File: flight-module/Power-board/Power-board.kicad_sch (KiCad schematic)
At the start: 26 parts, among them J5 POWER, J8 XT60-M, U1 AZ1117IH-3.3TRG1, U3 TPS4H160BQPWPRQ1, U4 AZ1117IH-5TRG1

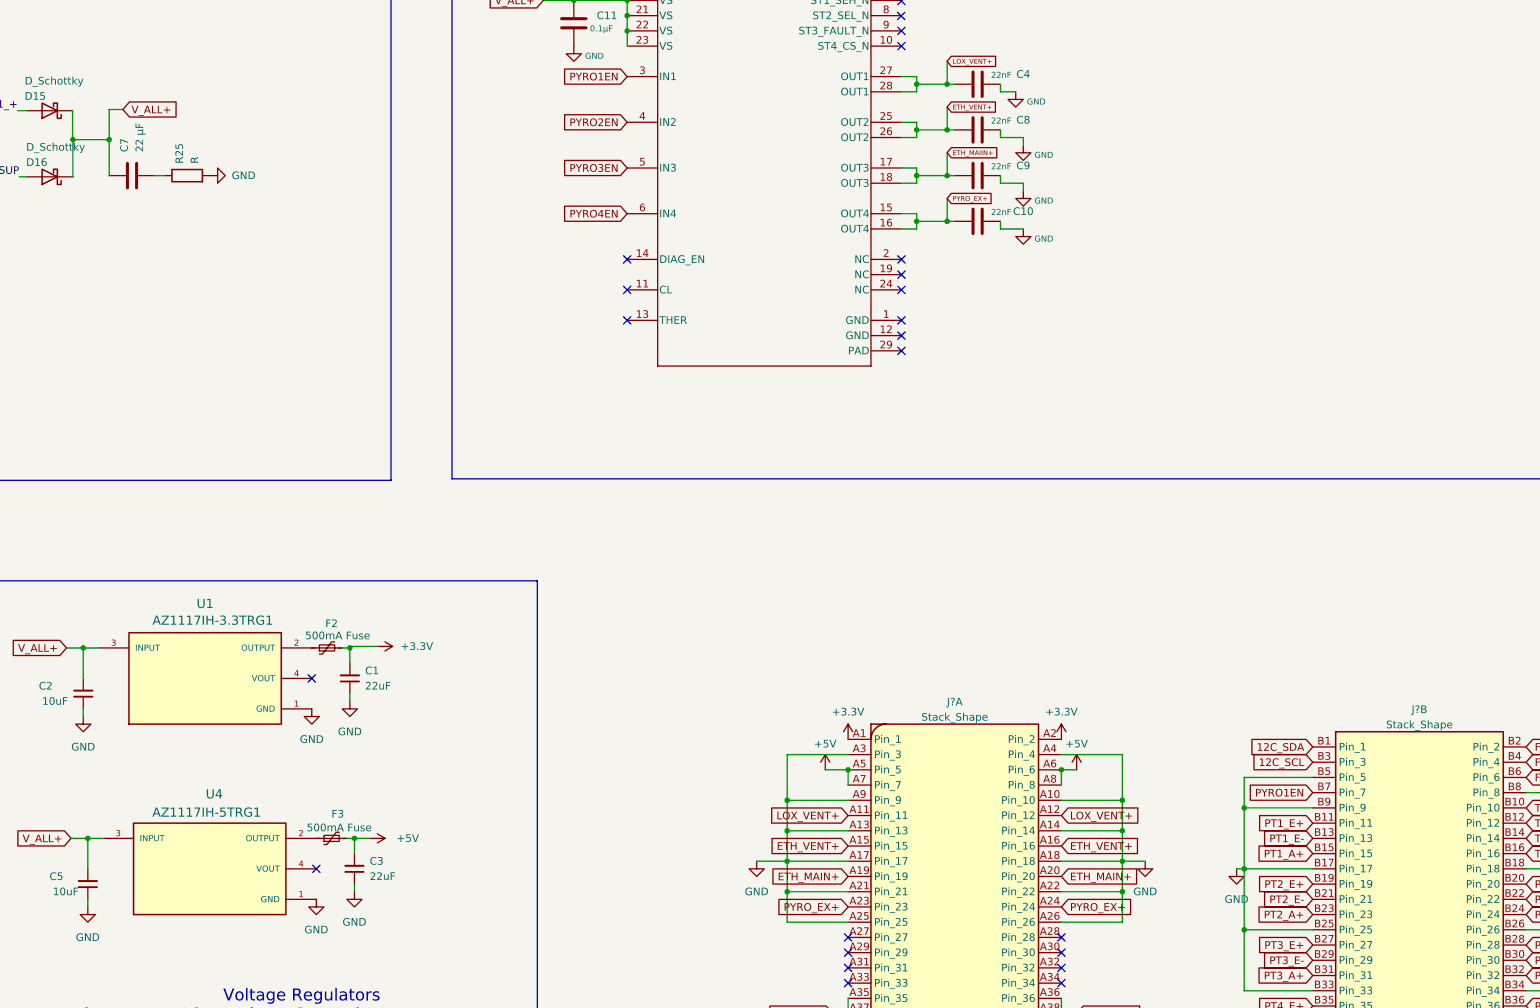
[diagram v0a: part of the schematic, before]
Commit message: added gnd to new ic on power board
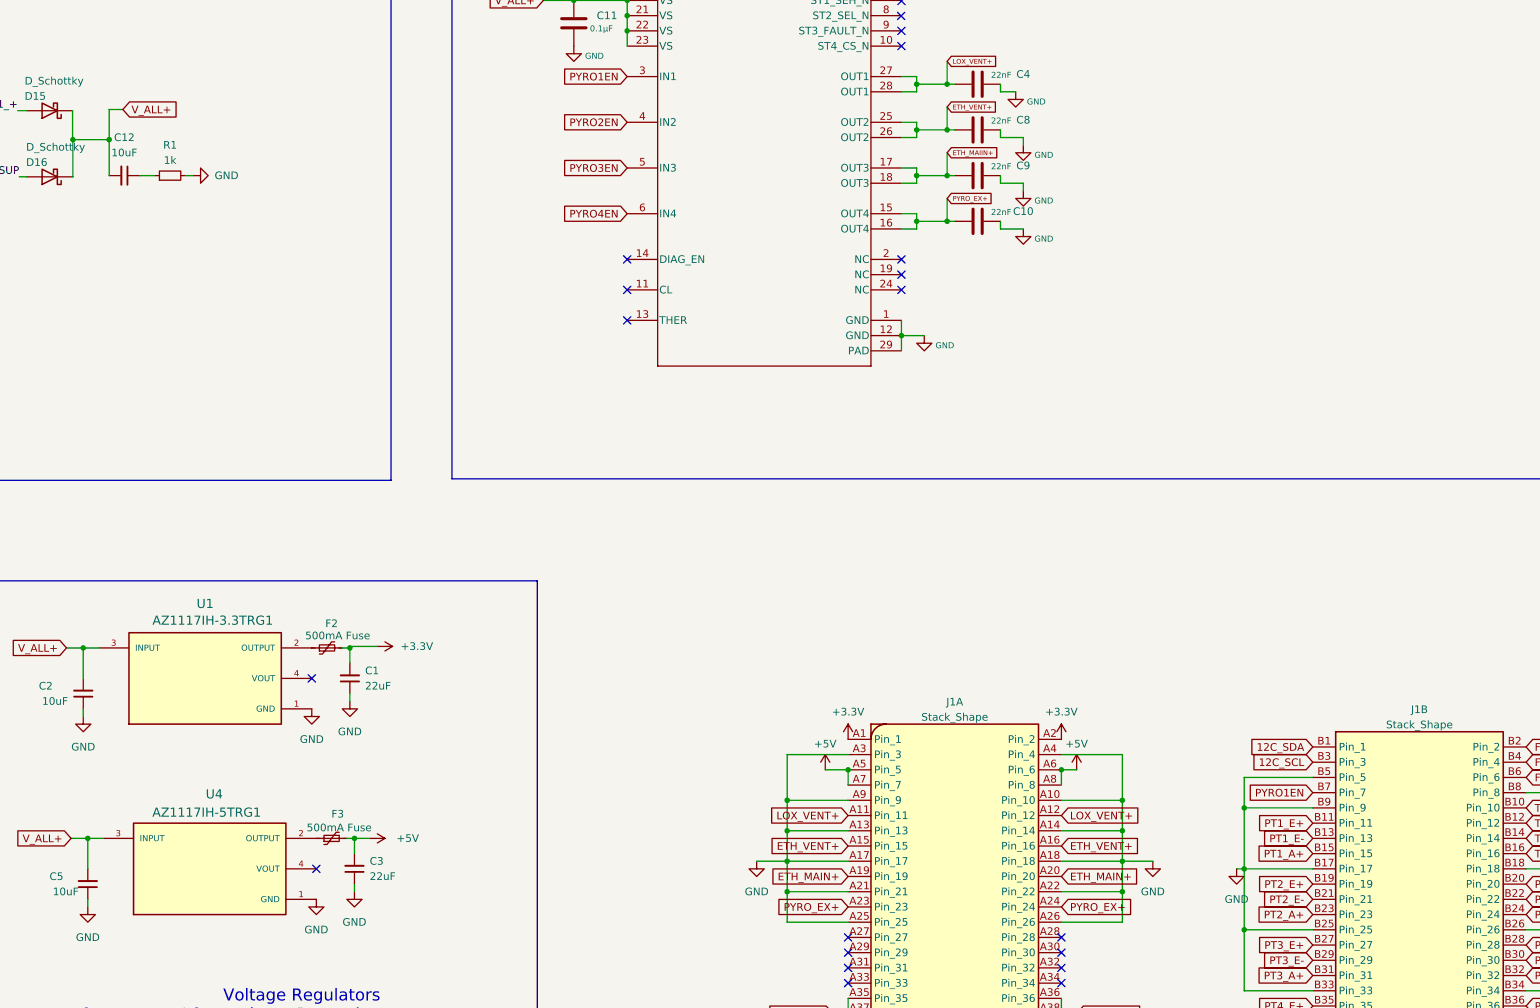
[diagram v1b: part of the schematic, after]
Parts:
- removed C7: 22 µF, symbol Device:C
- removed R25: R, symbol Device:R
- added C12: 10uF, Capacitor_SMD:C_0603_1608Metric, symbol Device:C_Small
- added R1: 1k, Resistor_SMD:R_0603_1608Metric, symbol Device:R_Small
- C10, C11, C4, C8, C9: footprint (none) -> Capacitor_SMD:C_0603_1608Metric
- D15, D16: footprint (none) -> Diode_SMD:D_0201_0603Metric
- U3: footprint PWP0028C_N -> TPS4:PWP0028C_N
- gave numbers to parts that had none: 1
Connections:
- net GND: now also U3.1 (GND), U3.12 (GND), U3.29 (PAD), R1.2
- net V_ALL+: now also C12.2
- new net: C12.1, R1.1
- no-connect marks 23 -> 20

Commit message: fixed a few erc errors on power board
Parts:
- J1: footprint (none) -> Stack_Shape:Stack_Shape
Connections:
- net 12C_SCL: no longer names the net of J1.B3 (Pin_3)
- net 12C_SDA: no longer names the net of J1.B1 (Pin_1)
- net FSPI_MISO: no longer names the net of J1.B4 (Pin_4)
- net FSPI_MOSI: no longer names the net of J1.B6 (Pin_6)
- net FSPI_SCK: no longer names the net of J1.B2 (Pin_2)
- net PT1_A+: no longer names the net of J1.B15 (Pin_15)
- net PT1_E+: no longer names the net of J1.B11 (Pin_11)
- net PT1_E-: no longer names the net of J1.B13 (Pin_13)
- net PT2_A+: no longer names the net of J1.B23 (Pin_23)
- net PT2_E+: no longer names the net of J1.B19 (Pin_19)
- net PT2_E-: no longer names the net of J1.B21 (Pin_21)
- net PT3_A+: no longer names the net of J1.B31 (Pin_31)
- net PT3_E+: no longer names the net of J1.B27 (Pin_27)
- net PT3_E-: no longer names the net of J1.B29 (Pin_29)
- net PT4_A+: no longer names the net of J1.B39 (Pin_39)
- net PT4_E+: no longer names the net of J1.B35 (Pin_35)
- net PT4_E-: no longer names the net of J1.B37 (Pin_37)
- net PT5_A+: no longer names the net of J1.B32 (Pin_32)
- net PT5_E+: no longer names the net of J1.B28 (Pin_28)
- net PT5_E-: no longer names the net of J1.B30 (Pin_30)
- net PT6_A+: no longer names the net of J1.B40 (Pin_40)
- net PT6_E+: no longer names the net of J1.B36 (Pin_36)
- net PT6_E-: no longer names the net of J1.B38 (Pin_38)
- net TC1_CS: no longer names the net of J1.B10 (Pin_10)
- net TC2_CS: no longer names the net of J1.B12 (Pin_12)
- net TC3_CS: no longer names the net of J1.B14 (Pin_14)
- net TC4_CS: no longer names the net of J1.B16 (Pin_16)
- no-connect marks 20 -> 47
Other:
- moved on the sheet: C1, C10, C11, C2, C3, C4, C5, C6, C8, C9, D15, D16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

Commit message: power board
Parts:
- U1, U4: footprint AZ1117IH-3:SOT230P700X185-4N -> AZ1117IH-3:SOT223_AZ1117I_6P5X3P5_DIO
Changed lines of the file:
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@@
+    )
+  )
+  (global_label "V_ALL+" (shape input) (at 180.34 195.58 180) (fields_autoplaced)
+    (effects (font (size 1.27 1.27)) (justify right))
+    (property "Intersheetrefs" "${INTERSHEET_REFS}" (at 170.5814 195.58 0)
+      (effects (font (size 1.27 1.27)) (justify right) hide)
     )
   )
@@
     (effects (font (size 1.27 1.27)) (justify right))
     (property "Intersheetrefs" "${INTERSHEET_REFS}" (at 249.3214 55.88 0)
-      (effects (font (size 1.27 1.27)) (justify right) hide)
-    )
-  )
-  (global_label "V_ALL+" (shape input) (at 180.34 195.58 180) (fields_autoplaced)
-    (effects (font (size 1.27 1.27)) (justify right))
-    (property "Intersheetrefs" "${INTERSHEET_REFS}" (at 170.5814 195.58 0)
       (effects (font (size 1.27 1.27)) (justify right) hide)
     )
@@
       (effects (font (size 1.524 1.524)))
     )
-    (property "Footprint" "AZ1117IH-3:SOT230P700X185-4N" (at 200.66 167.64 0)
+    (property "Footprint" "AZ1117IH-3:SOT223_AZ1117I_6P5X3P5_DIO" (at 200.66 167.64 0)
       (effects (font (size 1.27 1.27)) (justify bottom) hide)
     )
@@
       (effects (font (size 1.524 1.524)))
     )
-    (property "Footprint" "AZ1117IH-3:SOT230P700X185-4N" (at 203.2 200.66 0)
-      (effects (font (size 1.27 1.27)) (justify bottom) hide)
-    )
+    (property "Footprint" "AZ1117IH-3:SOT223_AZ1117I_6P5X3P5_DIO" (at 203.2 200.66 0)
+      (effects (font (size 1.27 1.27)) (justify bottom) hide)
+    )

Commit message: did some power board layout
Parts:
- D15, D16: footprint Diode_SMD:D_0201_0603Metric -> Diode_SMD:D_0603_1608Metric
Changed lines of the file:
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@@
       (effects (font (size 1.27 1.27)) (justify right))
     )
-    (property "Footprint" "Diode_SMD:D_0201_0603Metric" (at 176.53 83.82 0)
+    (property "Footprint" "Diode_SMD:D_0603_1608Metric" (at 176.53 83.82 0)
       (effects (font (size 1.27 1.27)) hide)
     )
@@
       (effects (font (size 1.27 1.27)) (justify right))
     )
-    (property "Footprint" "Diode_SMD:D_0201_0603Metric" (at 176.53 73.66 0)
+    (property "Footprint" "Diode_SMD:D_0603_1608Metric" (at 176.53 73.66 0)
       (effects (font (size 1.27 1.27)) hide)
     )

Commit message: some changes
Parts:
- D15, D16: footprint Diode_SMD:D_0603_1608Metric -> D_Schottky:SMADO-214AC_LEAD-FRAME_MCC
- J8: footprint XT60-M:AMASS_XT60-M -> Connector_AMASS:AMASS_XT60PW-F_1x02_P7.20mm_Horizontal
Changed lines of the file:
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@@
       (effects (font (size 1.27 1.27)) (justify left))
     )
-    (property "Footprint" "XT60-M:AMASS_XT60-M" (at 76.2 66.04 0)
+    (property "Footprint" "Connector_AMASS:AMASS_XT60PW-F_1x02_P7.20mm_Horizontal" (at 76.2 66.04 0)
       (effects (font (size 1.27 1.27)) (justify bottom) hide)
     )
@@
       (effects (font (size 1.27 1.27)) (justify right))
     )
-    (property "Footprint" "Diode_SMD:D_0603_1608Metric" (at 176.53 83.82 0)
+    (property "Footprint" "D_Schottky:SMADO-214AC_LEAD-FRAME_MCC" (at 176.53 83.82 0)
       (effects (font (size 1.27 1.27)) hide)
     )
@@
       (effects (font (size 1.27 1.27)) (justify right))
     )
-    (property "Footprint" "Diode_SMD:D_0603_1608Metric" (at 176.53 73.66 0)
-      (effects (font (size 1.27 1.27)) hide)
-    )
+    (property "Footprint" "D_Schottky:SMADO-214AC_LEAD-FRAME_MCC" (at 176.53 73.66 0)
+      (effects (font (size 1.27 1.27)) hide)
+    )

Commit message: routing not done
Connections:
- net BAT1_+_pre: now also J8.2; no longer J8.P (POS)
- net GND: now also J8.1; no longer J8.N (NEG)
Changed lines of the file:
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@@
       (effects (font (size 1.27 1.27)) (justify bottom) hide)
     )
-    (pin "N")
-    (pin "P")
+    (pin "2")
+    (pin "1")
     (instances
       (project "Power-board"
